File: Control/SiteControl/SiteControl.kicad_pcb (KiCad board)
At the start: 2 copper layers, 69 parts, among them J1 RJ50, P1 CONN_01X06, P2 USB_A, P3 CONN_01X02, Q1 BC817-40, U1 Opto_H11L1M, U2 Opto_H11L1M, U3 Opto_H11L1M, U4 Opto_H11L1M, U5 Opto_H11L1M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

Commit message: [Changed] RPi buck converter circuit to be lower power (1.8A)
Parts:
- removed C22: 0.1uF, Capacitors_SMD:C_0603
- removed HS1: HEATSINK, Heatsinks:Heatsink_Stonecold_HS-132_32x14mm_2xFixation1.5mm
- removed L2: 22uH, DigitalLogic:SRN1060-220M
- added Q2: Q_PJFET_GSD, TO_SOT_Packages_SMD:TO-252-2Lead, F.Cu at (356.7, 113.0)
- added R27: R18, Resistors_SMD:R_1206, F.Cu at (351.4, 104.7)
- added R28: 6K8, Resistors_SMD:R_0603, F.Cu at (406.9, 113.9)
- added R29: 2K2, Resistors_SMD:R_0603, F.Cu at (406.9, 116.5)
- C16: value 100uF -> 0.47uF; footprint Capacitors_SMD:c_elec_10x10 -> Capacitors_SMD:C_0805
- C17: value 1000uF -> 680uF
- C18: value 0.47uF -> 1nF; footprint Capacitors_SMD:C_0805 -> Capacitors_SMD:C_0603
- C19: value 0.47uF -> 1000uF; footprint Capacitors_SMD:C_0805 -> DigitalLogic:c_elec_13x13
- C2, C3, C4, C5: moved to B.Cu
- C20: value 100uF -> 0.47uF; footprint Capacitors_SMD:c_elec_6.3x7.7 -> Capacitors_SMD:C_0805
- C21: value 0.47uF -> 0.1uF; footprint Capacitors_SMD:C_0805 -> Capacitors_SMD:C_0603
- D1: value D_Schottky -> ~; footprint Diodes_SMD:DO-214AB_Handsoldering -> Diodes_SMD:DO-214AB
- R25: value Tie -> 560R; footprint Oddities:NetTie-I_Connected_SMD -> Resistors_SMD:R_0603
- R26: value 1K -> 10R; moved to F.Cu
- U9: value LM2576_Buck -> MC34063; footprint TO_SOT_Packages_THT:Pentawatt_Neutral_Straight_Vertical_TO220-5-T05A -> SO-8
- moved C21 188.9 mm to (410.5, 114.0), turned to 270 degrees
- moved C20 188.3 mm to (408.7, 114.4), turned to 270 degrees
- moved C19 153.6 mm to (397.9, 117.0), turned to 90 degrees
- moved L1 143.6 mm to (379.9, 112.0), turned to 180 degrees
- moved R26 113.5 mm to (351.5, 111.1), turned to 90 degrees
- moved R25 111.2 mm to (351.5, 113.7), turned to 90 degrees
- moved D1 101.1 mm to (353.3, 124.0), turned to 270 degrees
- moved C18 101.0 mm to (338.5, 110.6), turned to 270 degrees
- moved U9 74.1 mm to (343.5, 109.1)
- moved C17 73.3 mm to (326.9, 108.8), turned to 90 degrees
- moved C16 71.6 mm to (315.8, 109.4)
- moved C4 52.1 mm to (161.5, 64.9), turned to 90 degrees
- moved C3 47.0 mm to (165.5, 71.1), turned to 90 degrees
- moved C5 27.8 mm to (155.7, 71.2)
- moved C2 22.5 mm to (162.1, 76.2), turned to 90 degrees
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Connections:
- C16 pad 2: GNDD -> GND
- C17 pad 1: Net-(C17-Pad1) -> +BATT
- C17 pad 2: GNDD -> GND
- C18 pad 1: +BATT -> Net-(C18-Pad1)
- C19 pad 1: Net-(C17-Pad1) -> +5V
- C19 pad 2: GNDD -> GND
- D1 pad 2: GNDD -> GND
- L1 pad 2: Net-(C17-Pad1) -> +5V
- R25 pad 1: GNDD -> Net-(Q2-Pad3)
- R25 pad 2: GND -> Net-(Q2-Pad1)
- R26 pad 1: 5V_En -> Net-(Q2-Pad1)
- R26 pad 2: +3V3 -> Net-(R26-Pad2)
- U9 pad 1: +BATT -> Net-(R26-Pad2)
- U9 pad 2: Net-(D1-Pad1) -> GND
- U9 pad 3: GNDD -> Net-(C18-Pad1)
- U9 pad 4: Net-(C17-Pad1) -> GND
- U9 pad 5: 5V_En -> Net-(R28-Pad2)

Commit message: [WIP] Completed prelimary circuit and layout of the base control board
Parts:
- removed F1, F2: ATC-mini FUSE, Fuse_Holders_and_Fuses:Fuseholder_ATO_Blade_littlefuse_Pudenz_2_Pin
- added C22: 1uF/100V, Capacitors_SMD:C_1206, B.Cu at (122.7, 100.5)
- added C23: 0.22uF, Capacitors_SMD:C_0603, B.Cu at (115.0, 106.0)
- added C24: 10uF/6.3V, Capacitors_SMD:C_1206, B.Cu at (112.6, 102.9)
- added C25: 0.47uF, Capacitors_SMD:C_0603, B.Cu at (110.7, 101.9)
- added C26: 0.1uF, Capacitors_SMD:C_0603, B.Cu at (109.2, 101.9)
- added C27: 0.1uF, Capacitors_SMD:C_0603, F.Cu at (157.1, 78.5)
- added C28: 0.1uF, Capacitors_SMD:C_0603, B.Cu at (156.8, 83.1)
- added C29: 0.1uF, Capacitors_SMD:C_0603, B.Cu at (161.9, 83.3)
- added C30: 0.1uF, Capacitors_SMD:C_0603, F.Cu at (157.1, 81.7)
- added C31: 0.1uF, Capacitors_SMD:C_0603, F.Cu at (166.6, 77.1)
- added C32: 0.1uF, Capacitors_SMD:C_0603, B.Cu at (167.3, 86.6)
- added C33: 0.1uF, Capacitors_SMD:C_0603, B.Cu at (161.9, 78.5)
- added C34: 0.1uF, Resistors_SMD:R_0603, F.Cu at (122.7, 99.8)
- added C35: 0.1uF, Resistors_SMD:R_0603, F.Cu at (122.7, 93.0)
- added C36: 0.47uF/50V, Capacitors_SMD:C_0603, B.Cu at (121.9, 98.6)
- added L2: 150uH, DigitalLogic:SRR7045-151M_Inductor, F.Cu at (113.2, 101.1)
- added P4: CONN_01X02, Terminal_Blocks:TerminalBlock_Pheonix_MPT-2.54mm_2pol, F.Cu at (127.0, 107.8)
- added P5: CONN_02X04, Pin_Headers:Pin_Header_Straight_2x04, F.Cu at (119.0, 88.5)
- added P6: RS232-Jack, Connect:DB9FC, F.Cu at (161.9, 71.9)
- added P7: CONN_01X06, Pin_Headers:Pin_Header_Straight_1x06, F.Cu at (148.3, 88.3)
- added R30: 10K, Resistors_SMD:R_0603, F.Cu at (143.5, 76.8)
- added R31: 450R, Resistors_SMD:R_0603, F.Cu at (141.7, 76.8)
- added R32: 191K, Resistors_SMD:R_0603, B.Cu at (124.0, 104.0)
- added R33: 49K9, Resistors_SMD:R_0603, B.Cu at (122.9, 106.0)
- added R34: 158K, Resistors_SMD:R_0603, B.Cu at (120.4, 106.0)
- added R35: 22R1, Resistors_SMD:R_0603, B.Cu at (117.8, 106.0)
- added R36: 1K, Resistors_SMD:R_0603, B.Cu at (114.7, 103.0)
- added R37: 1K5, Resistors_SMD:R_0603, F.Cu at (119.3, 91.4)
- added R38: 1K5, Resistors_SMD:R_0603, F.Cu at (120.9, 91.4)
- added R39: R, Resistors_SMD:R_0603, B.Cu at (159.5, 68.6)
- added R40: 1K, Resistors_SMD:R_0603, F.Cu at (166.6, 79.9)
- added R41: 0R, Resistors_SMD:R_0603, F.Cu at (156.6, 75.9)
- added R42: 450R, Resistors_SMD:R_0603, F.Cu at (169.3, 75.4)
- added R43: 450R, Resistors_SMD:R_0603, F.Cu at (147.1, 77.2)
- added R44: 1M, Resistors_SMD:R_0805, F.Cu at (127.3, 99.4)
- added R45: 75K, Resistors_SMD:R_0805, F.Cu at (124.6, 100.0)
- added R46: 1K, Resistors_SMD:R_0603, F.Cu at (122.7, 96.8)
- added U10: SS_Relay_VO14642AT, DigitalLogic:SS_Relay_VO14642AT, F.Cu at (141.7, 84.6)
- added U11: MAX17552, DigitalLogic:MAX17552, B.Cu at (119.0, 103.3)
- added U12: ICL3221, SMD_Packages:SO-16-N, F.Cu at (161.8, 80.4)
- added U13: Opto_H11L1M, DigitalLogic:H11L1M, B.Cu at (151.6, 78.2)
- added U14: Opto_H11L1M, DigitalLogic:H11L1M, B.Cu at (168.7, 80.1)
- added U15: 12-Bit SPI ADC, SMD_Packages:SOIC-8-N, F.Cu at (126.2, 94.4)
- added W1: TEST_1P, Mounting_Holes:MountingHole_3.2mm_M3_Pad_Via, F.Cu at (112.9, 92.7)
- added W2: TEST_1P, Mounting_Holes:MountingHole_3.2mm_M3_Pad_Via, F.Cu at (139.3, 69.0)
- added W3: TEST_1P, Mounting_Holes:MountingHole_3.2mm_M3_Pad_Via, F.Cu at (182.9, 68.6)
- added W4: TEST_1P, Mounting_Holes:MountingHole_3.2mm_M3_Pad_Via, F.Cu at (184.2, 106.7)
- C1, C14, C18, R22, R24, R25, R26, R28, R29, U9: moved to B.Cu
- C16: value 0.47uF -> 0.47uF/50V
- R2: moved to F.Cu
- R20: value 100R -> 450R
- R21, R23: value 40R -> 450R; moved to B.Cu
- moved C20 227.5 mm to (182.6, 88.6), turned to 90 degrees
- moved C21 227.4 mm to (184.5, 88.2), turned to 90 degrees
- moved R28 219.7 mm to (188.5, 90.1), turned to 0 degrees
- moved R29 217.4 mm to (191.1, 90.1), turned to 0 degrees
- moved C19 210.7 mm to (188.2, 96.3)
- moved L1 208.1 mm to (172.3, 97.2), turned to 270 degrees
- moved Q2 203.9 mm to (153.5, 95.6)
- moved R25 202.3 mm to (150.1, 95.2), turned to 0 degrees
- moved R26 201.9 mm to (150.1, 96.9), turned to 180 degrees
- moved U9 199.4 mm to (144.7, 94.6), turned to 90 degrees
- moved C18 199.4 mm to (139.8, 93.3), turned to 90 degrees
- moved R27 197.8 mm to (153.7, 101.3), turned to 90 degrees
- moved D1 194.5 mm to (159.8, 104.4)
- moved C17 182.6 mm to (144.5, 99.4)
- moved C16 161.3 mm to (154.6, 104.5), turned to 0 degrees
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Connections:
- C16 pad 1: +BATT -> Net-(C16-Pad1)
- C17 pad 1: +BATT -> Net-(C16-Pad1)
- P2 pad 1: Net-(F1-Pad1) -> Net-(P2-Pad1)
- R27 pad 1: +BATT -> Net-(C16-Pad1)
- U7 pad 5: Net-(F2-Pad2) -> Net-(C14-Pad1)
- U8 pad 5: Net-(F1-Pad2) -> Net-(P2-Pad1)
- U9 pad 6: +BATT -> Net-(C16-Pad1)
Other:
- board outline added: 109.2 x 48.3 mm

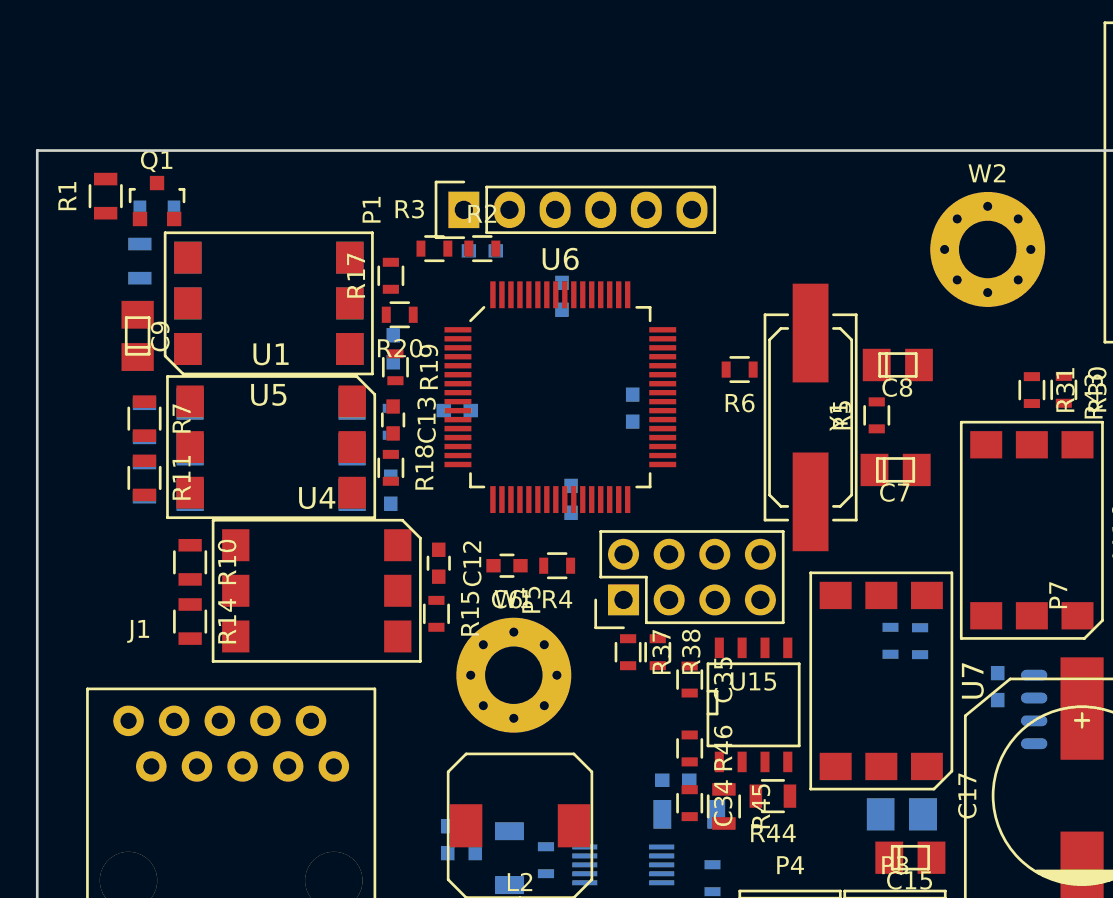
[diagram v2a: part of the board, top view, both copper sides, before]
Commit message: [Added] 3D models for parts on the base controller
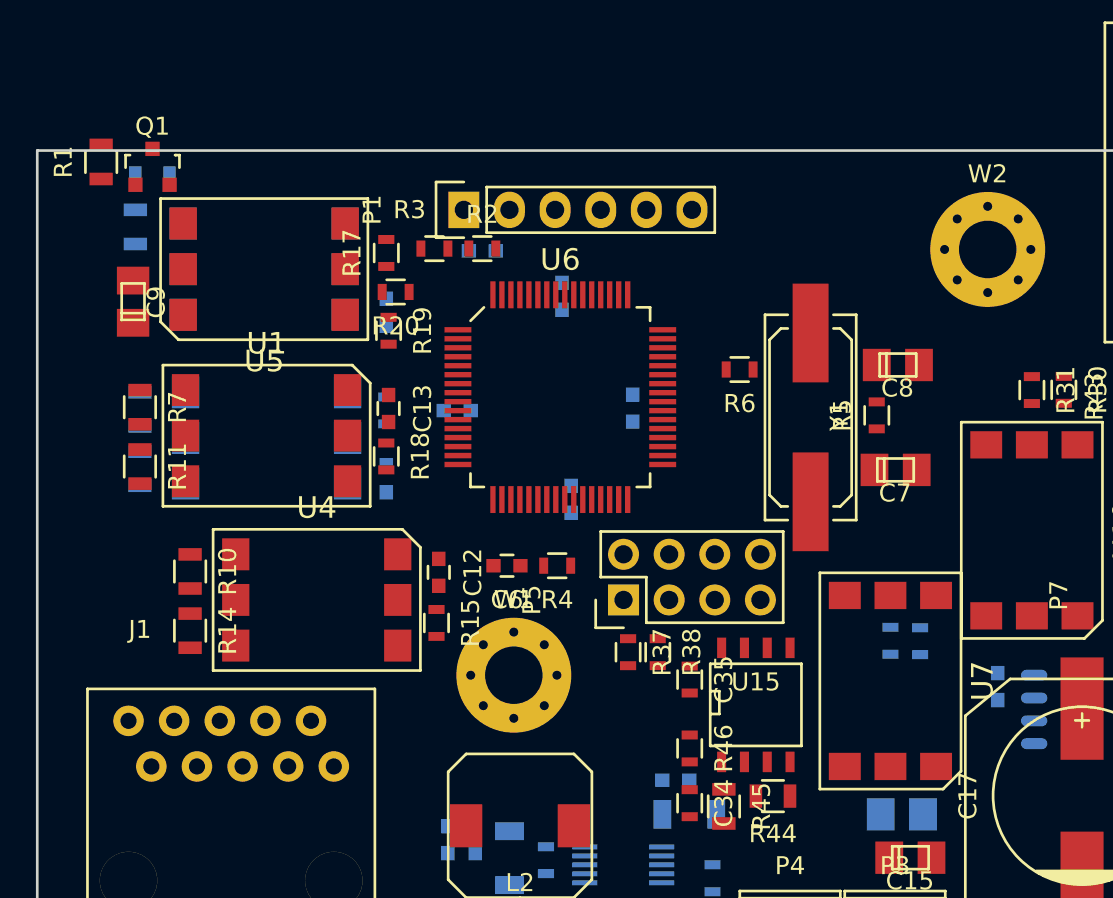
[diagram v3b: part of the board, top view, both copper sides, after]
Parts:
- moved C10 2.07 mm to (105.8, 72.5)
- moved R19 2.07 mm to (105.9, 73.5)
- moved Q1 1.92 mm to (92.8, 64.4)
- moved R1 1.92 mm to (89.9, 64.1)
- moved R12 1.92 mm to (91.8, 67.8)
- moved R8 1.92 mm to (92.8, 65.0)
- moved C9 1.92 mm to (91.7, 71.9)
- moved U2 1.92 mm to (99.0, 70.1)
- moved U5 1.92 mm to (99.0, 70.1)
- moved R17 1.30 mm to (105.8, 69.2)
- moved R20 1.29 mm to (106.3, 71.4)
- moved C11 0.68 mm to (105.8, 81.8)
- moved R16 0.68 mm to (105.8, 78.0)
- moved R18 0.68 mm to (105.8, 80.5)
- moved U1 0.68 mm to (99.1, 79.4)
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
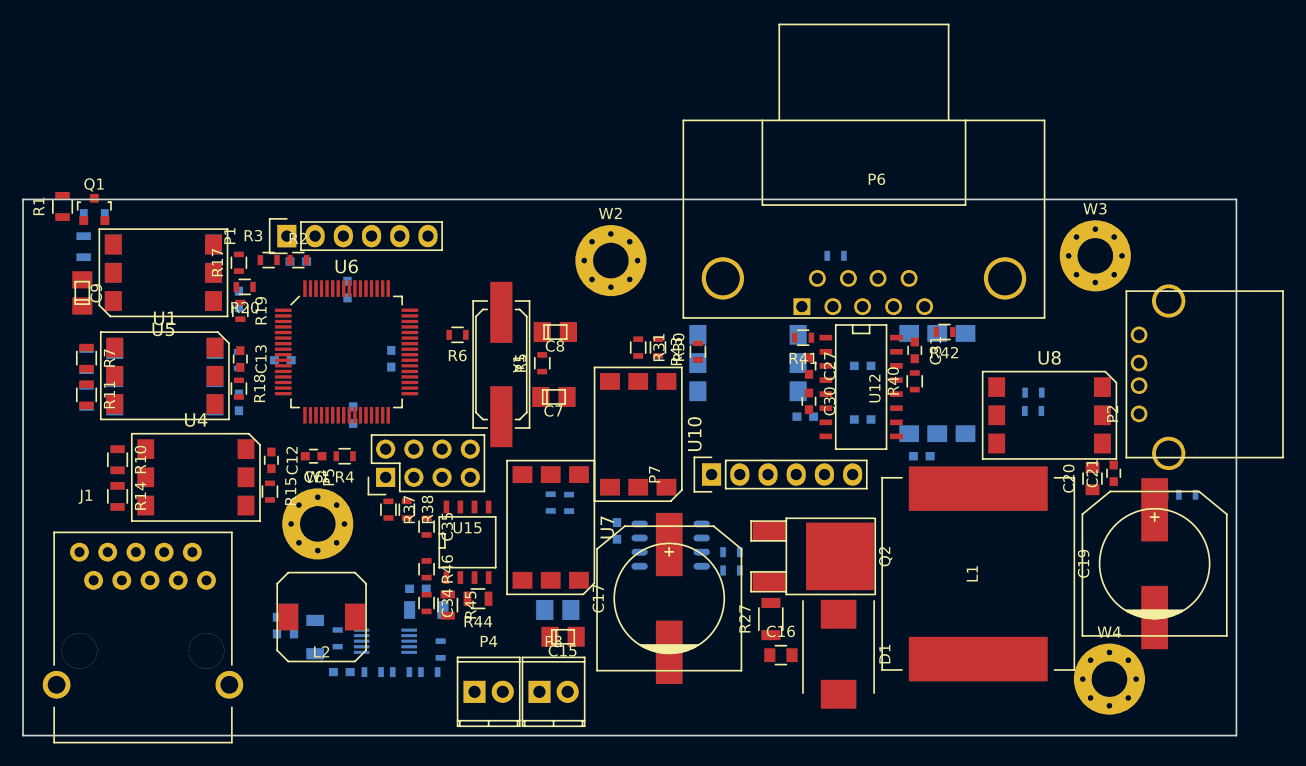
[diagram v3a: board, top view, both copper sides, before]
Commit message: [Added] more 3D models for the base control board. Rearanged parts a bit to allow for better clearance as per the 3D models
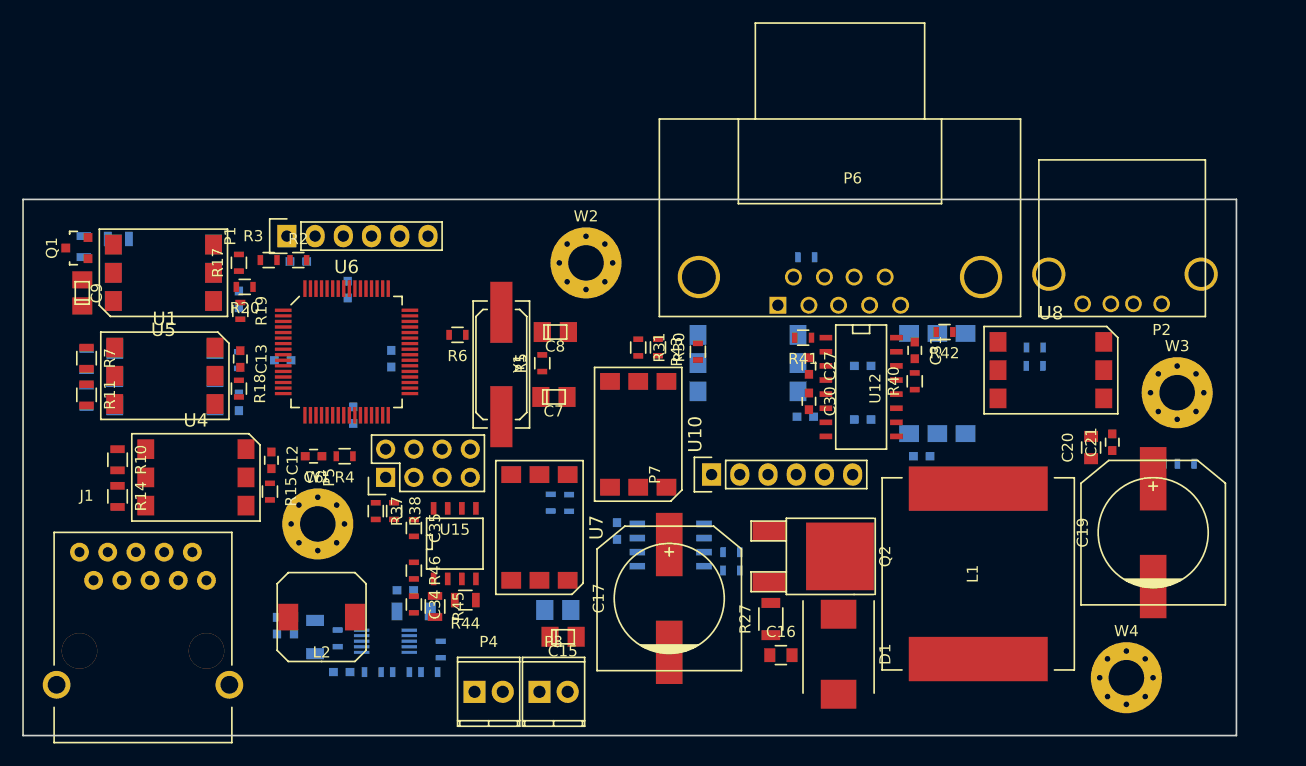
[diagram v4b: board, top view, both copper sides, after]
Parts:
- R1: moved to B.Cu
- U9: footprint SO-8 -> DigitalLogic:MC34063
- moved W3 14.4 mm to (190.2, 80.9)
- moved P2 10.1 mm to (188.8, 72.9), turned to 180 degrees
- moved R1 7.98 mm to (91.8, 71.9)
- moved R24 4.07 mm to (177.4, 76.8)
- moved R23 4.07 mm to (177.4, 78.5)
- moved U8 4.07 mm to (178.9, 78.9)
- moved Q1 3.81 mm to (91.2, 67.9), turned to 90 degrees
- moved R8 2.97 mm to (94.9, 67.1)
- moved C19 2.80 mm to (188.1, 93.5)
- moved C21 2.80 mm to (184.4, 85.4)
- moved C20 2.80 mm to (182.5, 85.8)
- moved R28 2.80 mm to (188.3, 87.3)
- moved R29 2.80 mm to (191.0, 87.3)
- moved R39 2.65 mm to (156.9, 68.7)
- moved W2 2.25 mm to (137.0, 69.2)
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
